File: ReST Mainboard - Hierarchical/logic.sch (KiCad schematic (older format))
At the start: 21 parts, among them IC1 AT24C256, P15 USB_OTG, P40 CONN_02X04, U10 USBLC6-2, U9 STM32F10x/STM32F4x, X1 Crystal_Small

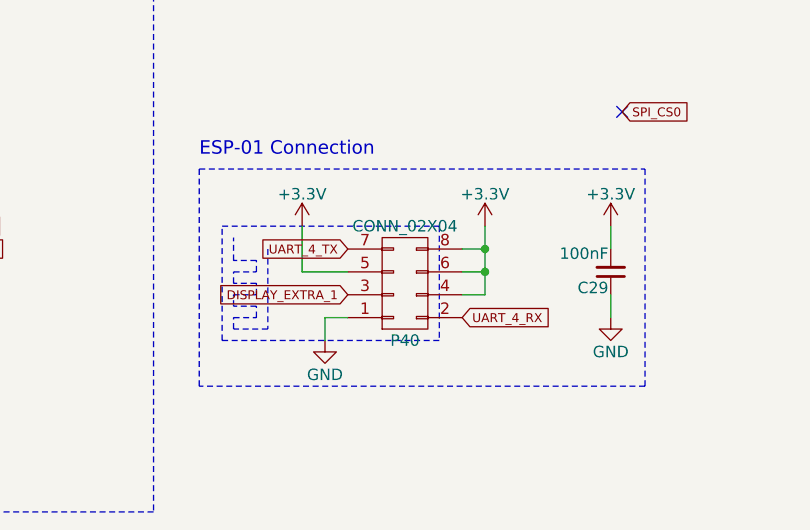
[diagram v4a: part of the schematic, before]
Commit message: Added ESP To the Mainboard
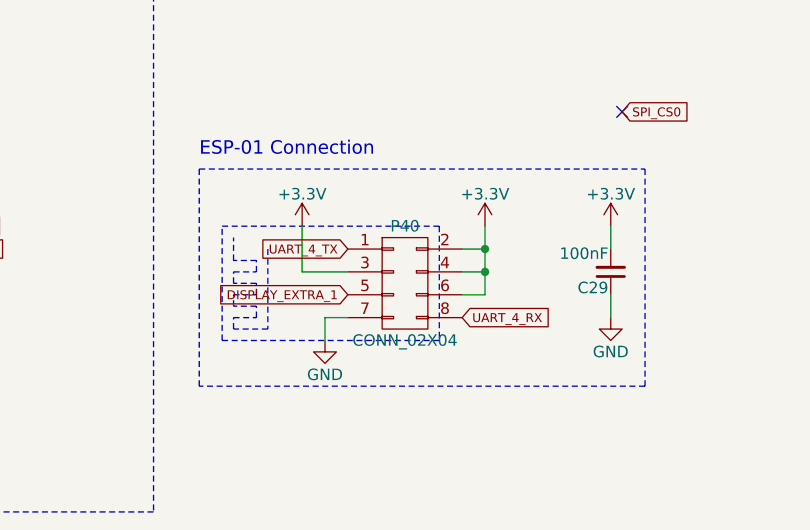
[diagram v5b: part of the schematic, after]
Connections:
- net +3V3: now also P40.2 (P2), P40.3 (P3); no longer P40.5 (P5), P40.8 (P8)
- net DISPLAY_EXTRA_1: now also P40.5 (P5); no longer P40.3 (P3)
- net GND: now also P40.7 (P7); no longer P40.1 (P1)
- net UART_4_RX: now also P40.8 (P8); no longer P40.2 (P2)
- net UART_4_TX: now also P40.1 (P1); no longer P40.7 (P7)
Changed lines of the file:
@@
 $EndDescr
 $Comp
-L +3.3V #PWR121
+L +3.3V #PWR0120
 U 1 1 5778C1BC
 P 8400 3200
-F 0 "#PWR121" H 8400 3050 50  0001 C CNN
+F 0 "#PWR0120" H 8400 3050 50  0001 C CNN
 F 1 "+3.3V" H 8400 3340 50  0000 C CNN
 F 2 "" H 8400 3200 50  0000 C CNN
@@
 $EndComp
 $Comp
-L GND #PWR122
+L GND #PWR0121
 U 1 1 5778C1C2
 P 8400 3800
-F 0 "#PWR122" H 8400 3550 50  0001 C CNN
+F 0 "#PWR0121" H 8400 3550 50  0001 C CNN
 F 1 "GND" H 8400 3650 50  0000 C CNN
 F 2 "" H 8400 3800 50  0000 C CNN
@@
 I2C_SDA
 $Comp
-L +3.3V #PWR131
+L +3.3V #PWR0122
 U 1 1 5778E907
 P 10800 2950
-F 0 "#PWR131" H 10800 2800 50  0001 C CNN
+F 0 "#PWR0122" H 10800 2800 50  0001 C CNN
 F 1 "+3.3V" H 10800 3090 50  0000 C CNN
 F 2 "" H 10800 2950 50  0000 C CNN
@@
 I2C_SDA
 $Comp
-L +3V3 #PWR119
+L +3V3 #PWR0123
 U 1 1 57791FB8
 P 5000 -150
-F 0 "#PWR119" H 5000 -300 50  0001 C CNN
+F 0 "#PWR0123" H 5000 -300 50  0001 C CNN
 F 1 "+3V3" H 5000 -10 50  0000 C CNN
 F 2 "" H 5000 -150 50  0000 C CNN
@@
 $EndComp
 $Comp
-L GND #PWR116
+L GND #PWR0124
 U 1 1 57791FBE
 P 3050 1050
-F 0 "#PWR116" H 3050 800 50  0001 C CNN
+F 0 "#PWR0124" H 3050 800 50  0001 C CNN
 F 1 "GND" H 3050 900 50  0000 C CNN
 F 2 "" H 3050 1050 50  0000 C CNN
@@
 $EndComp
 $Comp
-L GND #PWR120
+L GND #PWR0125
 U 1 1 57791FC4
 P 5200 6150
-F 0 "#PWR120" H 5200 5900 50  0001 C CNN
+F 0 "#PWR0125" H 5200 5900 50  0001 C CNN
 F 1 "GND" H 5200 6000 50  0000 C CNN
 F 2 "" H 5200 6150 50  0000 C CNN
@@
 $EndComp
 $Comp
-L GND #PWR118
+L GND #PWR0126
 U 1 1 57791FDF
 P 3600 1950
-F 0 "#PWR118" H 3600 1700 50  0001 C CNN
+F 0 "#PWR0126" H 3600 1700 50  0001 C CNN
 F 1 "GND" H 3600 1800 50  0000 C CNN
 F 2 "" H 3600 1950 50  0000 C CNN
@@
 $EndComp
 $Comp
-L +3V3 #PWR117
+L +3V3 #PWR0127
 U 1 1 57791FED
 P 3600 150
-F 0 "#PWR117" H 3600 0   50  0001 C CNN
+F 0 "#PWR0127" H 3600 0   50  0001 C CNN
 F 1 "+3V3" H 3600 290 50  0000 C CNN
 F 2 "" H 3600 150 50  0000 C CNN
@@
 $EndComp
 $Comp
-L GND #PWR113
+L GND #PWR0128
 U 1 1 57791FF3
 P 2600 650
-F 0 "#PWR113" H 2600 400 50  0001 C CNN
+F 0 "#PWR0128" H 2600 400 50  0001 C CNN
 F 1 "GND" H 2600 500 50  0000 C CNN
 F 2 "" H 2600 650 50  0000 C CNN
@@
 $EndComp
 $Comp
-L +3V3 #PWR115
+L +3V3 #PWR0129
 U 1 1 57792016
 P 3000 2450
-F 0 "#PWR115" H 3000 2300 50  0001 C CNN
+F 0 "#PWR0129" H 3000 2300 50  0001 C CNN
 F 1 "+3V3" H 3000 2590 50  0000 C CNN
 F 2 "" H 3000 2450 50  0000 C CNN
@@
 $EndComp
 $Comp
-L GND #PWR114
+L GND #PWR0130
 U 1 1 5779201C
 P 3000 1400
-F 0 "#PWR114" H 3000 1150 50  0001 C CNN
+F 0 "#PWR0130" H 3000 1150 50  0001 C CNN
 F 1 "GND" H 3000 1250 50  0000 C CNN
 F 2 "" H 3000 1400 50  0000 C CNN
@@
 $EndComp
 $Comp
-L GND #PWR126
+L GND #PWR0131
 U 1 1 577937EA
 P 9100 1350
-F 0 "#PWR126" H 9100 1100 50  0001 C CNN
+F 0 "#PWR0131" H 9100 1100 50  0001 C CNN
 F 1 "GND" H 9100 1200 50  0000 C CNN
 F 2 "" H 9100 1350 50  0000 C CNN
@@
 $EndComp
 $Comp
-L VCC #PWR125
+L VCC #PWR0132
 U 1 1 57793807
 P 9100 250
-F 0 "#PWR125" H 9100 100 50  0001 C CNN
+F 0 "#PWR0132" H 9100 100 50  0001 C CNN
 F 1 "VCC" H 9100 400 50  0000 C CNN
 F 2 "" H 9100 250 50  0000 C CNN
@@
 $EndComp
 $Comp
-L VCC #PWR130
+L VCC #PWR0133
 U 1 1 5779380D
 P 10400 750
-F 0 "#PWR130" H 10400 600 50  0001 C CNN
+F 0 "#PWR0133" H 10400 600 50  0001 C CNN
 F 1 "VCC" H 10400 900 50  0000 C CNN
 F 2 "" H 10400 750 50  0000 C CNN
@@
 F 3 "" H 8850 4200 50  0000 C CNN
 	1    8850 5400
-	1    0    0    1
-$EndComp
-$Comp
-L +3.3V #PWR127
+	1    0    0    -1
+$EndComp
+$Comp
+L +3.3V #PWR0134
 U 1 1 5797FE7C
 P 9200 5150
-F 0 "#PWR127" H 9200 5000 50  0001 C CNN
+F 0 "#PWR0134" H 9200 5000 50  0001 C CNN
 F 1 "+3.3V" H 9200 5290 50  0000 C CNN
 F 2 "" H 9200 5150 50  0000 C CNN
@@
 $EndComp
 $Comp
-L GND #PWR124
+L GND #PWR0135
 U 1 1 5797FEC3
 P 8500 5650
-F 0 "#PWR124" H 8500 5400 50  0001 C CNN
+F 0 "#PWR0135" H 8500 5400 50  0001 C CNN
 F 1 "GND" H 8500 5500 50  0000 C CNN
 F 2 "" H 8500 5650 50  0000 C CNN
@@
 NoConn ~ 9800 4650
 $Comp
-L +3.3V #PWR128
+L +3.3V #PWR0136
 U 1 1 57980B54
 P 9750 5150
-F 0 "#PWR128" H 9750 5000 50  0001 C CNN
+F 0 "#PWR0136" H 9750 5000 50  0001 C CNN
 F 1 "+3.3V" H 9750 5290 50  0000 C CNN
 F 2 "" H 9750 5150 50  0000 C CNN
@@
 $EndComp
 $Comp
-L GND #PWR129
+L GND #PWR0137
 U 1 1 57980B9E
 P 9750 5550
-F 0 "#PWR129" H 9750 5300 50  0001 C CNN
+F 0 "#PWR0137" H 9750 5300 50  0001 C CNN
 F 1 "GND" H 9750 5400 50  0000 C CNN
 F 2 "" H 9750 5550 50  0000 C CNN
@@
 	8400 5350 8600 5350
 $Comp
-L +3.3V #PWR123
+L +3.3V #PWR0138
 U 1 1 57983B6D
 P 8400 5150
-F 0 "#PWR123" H 8400 5000 50  0001 C CNN
+F 0 "#PWR0138" H 8400 5000 50  0001 C CNN
 F 1 "+3.3V" H 8400 5290 50  0000 C CNN
 F 2 "" H 8400 5150 50  0000 C CNN

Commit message: added missing usb pullup
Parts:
- added R24: 1K5, Resistors_SMD:R_0805_HandSoldering, symbol R_Small
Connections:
- net +3V3: now also R24.2
- net USBP_D+: now also R24.1
- no-connect marks 8 -> 9
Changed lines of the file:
@@
 Text Notes 7950 4850 0    59   ~ 0
 ESP-01 Connection
+$Comp
+L R_Small R24
+U 1 1 5798C112
+P 9750 1150
+F 0 "R24" H 9780 1170 50  0000 L CNN
+F 1 "1K5" H 9780 1110 50  0000 L CNN
+F 2 "Resistors_SMD:R_0805_HandSoldering" H 9750 1150 50  0001 C CNN
+F 3 "" H 9750 1150 50  0000 C CNN
+	1    9750 1150
+	-1   0    0    1
+$EndComp
+$Comp
+L +3.3V #PWR0139
+U 1 1 5798C54C
+P 9750 1000
+F 0 "#PWR0139" H 9750 850 50  0001 C CNN
+F 1 "+3.3V" H 9750 1140 50  0000 C CNN
+F 2 "" H 9750 1000 50  0000 C CNN
+F 3 "" H 9750 1000 50  0000 C CNN
+	1    9750 1000
+	1    0    0    -1
+$EndComp
+Wire Wire Line
+	9750 1000 9750 1050
+Text Label 9750 1250 3    39   ~ 0
+USBP_D+
+NoConn ~ 3400 650
 $EndSCHEMATC

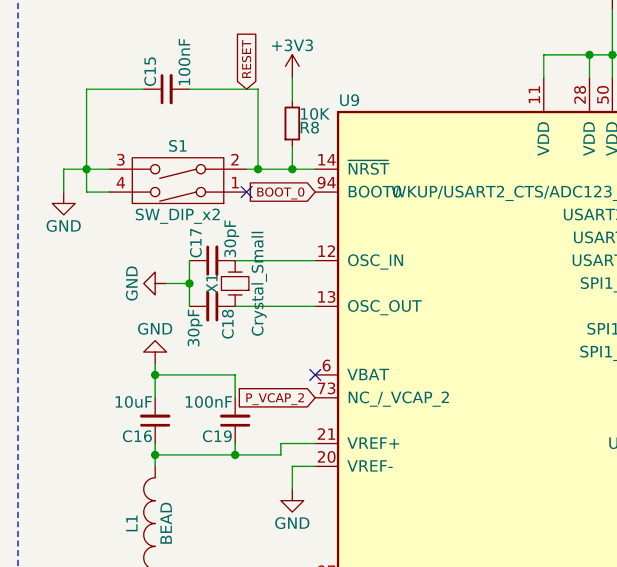
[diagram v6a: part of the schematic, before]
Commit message: minor changes to values of components and footprints. added two leds for both 12V Rails.
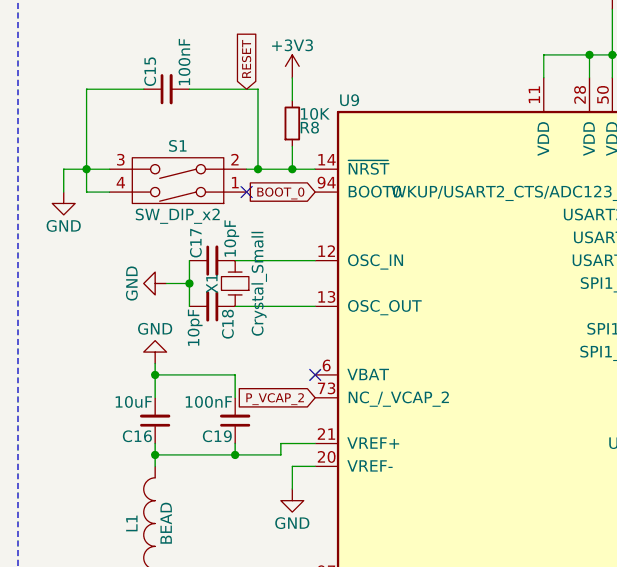
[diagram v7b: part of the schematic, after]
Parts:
- C17, C18: value 30pF -> 10pF
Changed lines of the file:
@@
 $EndDescr
 $Comp
-L +3.3V #PWR0120
+L +3.3V #PWR0124
 U 1 1 5778C1BC
 P 8400 3200
-F 0 "#PWR0120" H 8400 3050 50  0001 C CNN
+F 0 "#PWR0124" H 8400 3050 50  0001 C CNN
 F 1 "+3.3V" H 8400 3340 50  0000 C CNN
 F 2 "" H 8400 3200 50  0000 C CNN
@@
 $EndComp
 $Comp
-L GND #PWR0121
+L GND #PWR0125
 U 1 1 5778C1C2
 P 8400 3800
-F 0 "#PWR0121" H 8400 3550 50  0001 C CNN
+F 0 "#PWR0125" H 8400 3550 50  0001 C CNN
 F 1 "GND" H 8400 3650 50  0000 C CNN
 F 2 "" H 8400 3800 50  0000 C CNN
@@
 I2C_SDA
 $Comp
-L +3.3V #PWR0122
+L +3.3V #PWR0126
 U 1 1 5778E907
 P 10800 2950
-F 0 "#PWR0122" H 10800 2800 50  0001 C CNN
+F 0 "#PWR0126" H 10800 2800 50  0001 C CNN
 F 1 "+3.3V" H 10800 3090 50  0000 C CNN
 F 2 "" H 10800 2950 50  0000 C CNN
@@
 I2C_SDA
 $Comp
-L +3V3 #PWR0123
+L +3V3 #PWR0127
 U 1 1 57791FB8
 P 5000 -150
-F 0 "#PWR0123" H 5000 -300 50  0001 C CNN
+F 0 "#PWR0127" H 5000 -300 50  0001 C CNN
 F 1 "+3V3" H 5000 -10 50  0000 C CNN
 F 2 "" H 5000 -150 50  0000 C CNN
@@
 $EndComp
 $Comp
-L GND #PWR0124
+L GND #PWR0128
 U 1 1 57791FBE
 P 3050 1050
-F 0 "#PWR0124" H 3050 800 50  0001 C CNN
+F 0 "#PWR0128" H 3050 800 50  0001 C CNN
 F 1 "GND" H 3050 900 50  0000 C CNN
 F 2 "" H 3050 1050 50  0000 C CNN
@@
 $EndComp
 $Comp
-L GND #PWR0125
+L GND #PWR0129
 U 1 1 57791FC4
 P 5200 6150
-F 0 "#PWR0125" H 5200 5900 50  0001 C CNN
+F 0 "#PWR0129" H 5200 5900 50  0001 C CNN
 F 1 "GND" H 5200 6000 50  0000 C CNN
 F 2 "" H 5200 6150 50  0000 C CNN
@@
 $EndComp
 $Comp
-L GND #PWR0126
+L GND #PWR0130
 U 1 1 57791FDF
 P 3600 1950
-F 0 "#PWR0126" H 3600 1700 50  0001 C CNN
+F 0 "#PWR0130" H 3600 1700 50  0001 C CNN
 F 1 "GND" H 3600 1800 50  0000 C CNN
 F 2 "" H 3600 1950 50  0000 C CNN
@@
 $EndComp
 $Comp
-L +3V3 #PWR0127
+L +3V3 #PWR0131
 U 1 1 57791FED
 P 3600 150
-F 0 "#PWR0127" H 3600 0   50  0001 C CNN
+F 0 "#PWR0131" H 3600 0   50  0001 C CNN
 F 1 "+3V3" H 3600 290 50  0000 C CNN
 F 2 "" H 3600 150 50  0000 C CNN
@@
 $EndComp
 $Comp
-L GND #PWR0128
+L GND #PWR0132
 U 1 1 57791FF3
 P 2600 650
-F 0 "#PWR0128" H 2600 400 50  0001 C CNN
+F 0 "#PWR0132" H 2600 400 50  0001 C CNN
 F 1 "GND" H 2600 500 50  0000 C CNN
 F 2 "" H 2600 650 50  0000 C CNN
@@
 P 3250 1150
 F 0 "C18" H 3260 1220 50  0000 L CNN
-F 1 "30pF" H 3260 1070 50  0000 L CNN
+F 1 "10pF" H 3260 1070 50  0000 L CNN
 F 2 "Resistors_SMD:R_0805_HandSoldering" H 3250 1150 50  0001 C CNN
 F 3 "" H 3250 1150 50  0000 C CNN
@@
 P 3250 950
 F 0 "C17" H 3260 1020 50  0000 L CNN
-F 1 "30pF" H 3260 870 50  0000 L CNN
+F 1 "10pF" H 3260 870 50  0000 L CNN
 F 2 "Resistors_SMD:R_0805_HandSoldering" H 3250 950 50  0001 C CNN
 F 3 "" H 3250 950 50  0000 C CNN
@@
 $EndComp
 $Comp
-L +3V3 #PWR0129
+L +3V3 #PWR0133
 U 1 1 57792016
 P 3000 2450
-F 0 "#PWR0129" H 3000 2300 50  0001 C CNN
+F 0 "#PWR0133" H 3000 2300 50  0001 C CNN
 F 1 "+3V3" H 3000 2590 50  0000 C CNN
 F 2 "" H 3000 2450 50  0000 C CNN
@@
 $EndComp
 $Comp
-L GND #PWR0130
+L GND #PWR0134
 U 1 1 5779201C
 P 3000 1400
-F 0 "#PWR0130" H 3000 1150 50  0001 C CNN
+F 0 "#PWR0134" H 3000 1150 50  0001 C CNN
 F 1 "GND" H 3000 1250 50  0000 C CNN
 F 2 "" H 3000 1400 50  0000 C CNN
@@
 $EndComp
 $Comp
-L GND #PWR0131
+L GND #PWR0135
 U 1 1 577937EA
 P 9100 1350
-F 0 "#PWR0131" H 9100 1100 50  0001 C CNN
+F 0 "#PWR0135" H 9100 1100 50  0001 C CNN
 F 1 "GND" H 9100 1200 50  0000 C CNN
 F 2 "" H 9100 1350 50  0000 C CNN
@@
 $EndComp
 $Comp
-L VCC #PWR0132
+L VCC #PWR0136
 U 1 1 57793807
 P 9100 250
-F 0 "#PWR0132" H 9100 100 50  0001 C CNN
+F 0 "#PWR0136" H 9100 100 50  0001 C CNN
 F 1 "VCC" H 9100 400 50  0000 C CNN
 F 2 "" H 9100 250 50  0000 C CNN
@@
 $EndComp
 $Comp
-L VCC #PWR0133
+L VCC #PWR0137
 U 1 1 5779380D
 P 10400 750
-F 0 "#PWR0133" H 10400 600 50  0001 C CNN
+F 0 "#PWR0137" H 10400 600 50  0001 C CNN
 F 1 "VCC" H 10400 900 50  0000 C CNN
 F 2 "" H 10400 750 50  0000 C CNN
@@
 $EndComp
 $Comp
-L +3.3V #PWR0134
+L +3.3V #PWR0138
 U 1 1 5797FE7C
 P 9200 5150
-F 0 "#PWR0134" H 9200 5000 50  0001 C CNN
+F 0 "#PWR0138" H 9200 5000 50  0001 C CNN
 F 1 "+3.3V" H 9200 5290 50  0000 C CNN
 F 2 "" H 9200 5150 50  0000 C CNN
@@
 $EndComp
 $Comp
-L GND #PWR0135
+L GND #PWR0139
 U 1 1 5797FEC3
 P 8500 5650
-F 0 "#PWR0135" H 8500 5400 50  0001 C CNN
+F 0 "#PWR0139" H 8500 5400 50  0001 C CNN
 F 1 "GND" H 8500 5500 50  0000 C CNN
 F 2 "" H 8500 5650 50  0000 C CNN
@@
 NoConn ~ 9800 4650
 $Comp
-L +3.3V #PWR0136
+L +3.3V #PWR0140
 U 1 1 57980B54
 P 9750 5150
-F 0 "#PWR0136" H 9750 5000 50  0001 C CNN
+F 0 "#PWR0140" H 9750 5000 50  0001 C CNN
 F 1 "+3.3V" H 9750 5290 50  0000 C CNN
 F 2 "" H 9750 5150 50  0000 C CNN
@@
 $EndComp
 $Comp
-L GND #PWR0137
+L GND #PWR0141
 U 1 1 57980B9E
 P 9750 5550
-F 0 "#PWR0137" H 9750 5300 50  0001 C CNN
+F 0 "#PWR0141" H 9750 5300 50  0001 C CNN
 F 1 "GND" H 9750 5400 50  0000 C CNN
 F 2 "" H 9750 5550 50  0000 C CNN
@@
 	8400 5350 8600 5350
 $Comp
-L +3.3V #PWR0138
+L +3.3V #PWR0142
 U 1 1 57983B6D
 P 8400 5150
-F 0 "#PWR0138" H 8400 5000 50  0001 C CNN
+F 0 "#PWR0142" H 8400 5000 50  0001 C CNN
 F 1 "+3.3V" H 8400 5290 50  0000 C CNN
 F 2 "" H 8400 5150 50  0000 C CNN
@@
 $EndComp
 $Comp
-L +3.3V #PWR0139
+L +3.3V #PWR0143
 U 1 1 5798C54C
 P 9750 1000
-F 0 "#PWR0139" H 9750 850 50  0001 C CNN
+F 0 "#PWR0143" H 9750 850 50  0001 C CNN
 F 1 "+3.3V" H 9750 1140 50  0000 C CNN
 F 2 "" H 9750 1000 50  0000 C CNN
